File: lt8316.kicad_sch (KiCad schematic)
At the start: 37 parts

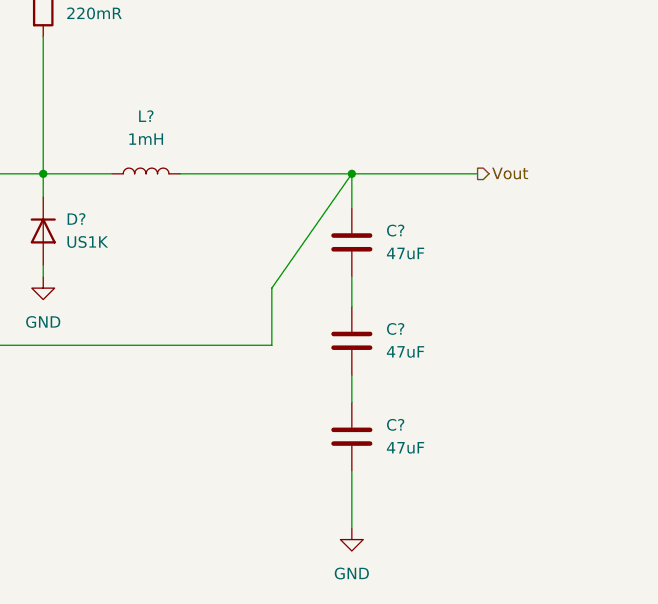
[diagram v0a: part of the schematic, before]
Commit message: gitignore change + capacitors improve
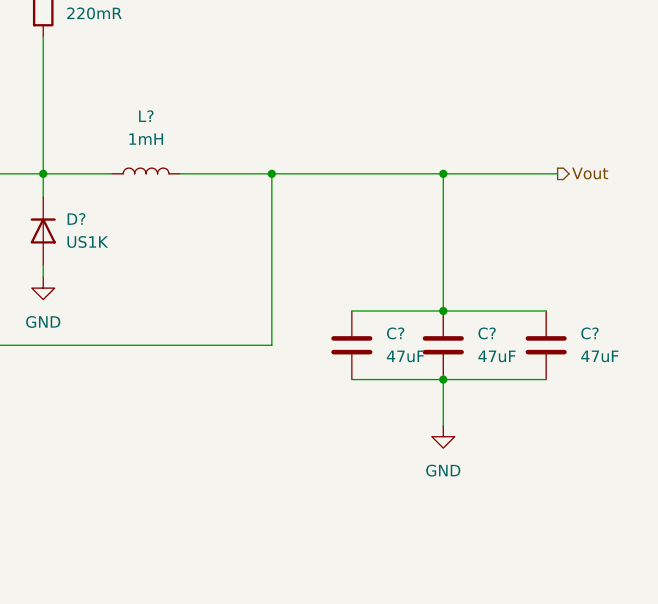
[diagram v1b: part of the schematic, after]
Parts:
- removed C?: 47uF, symbol Device:C
- added C?: 47uF, symbol Device:C
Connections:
- net GND: now also C?.2, C?.2
- net Vout: now also C?.1, C?.1
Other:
- moved on the sheet: C?

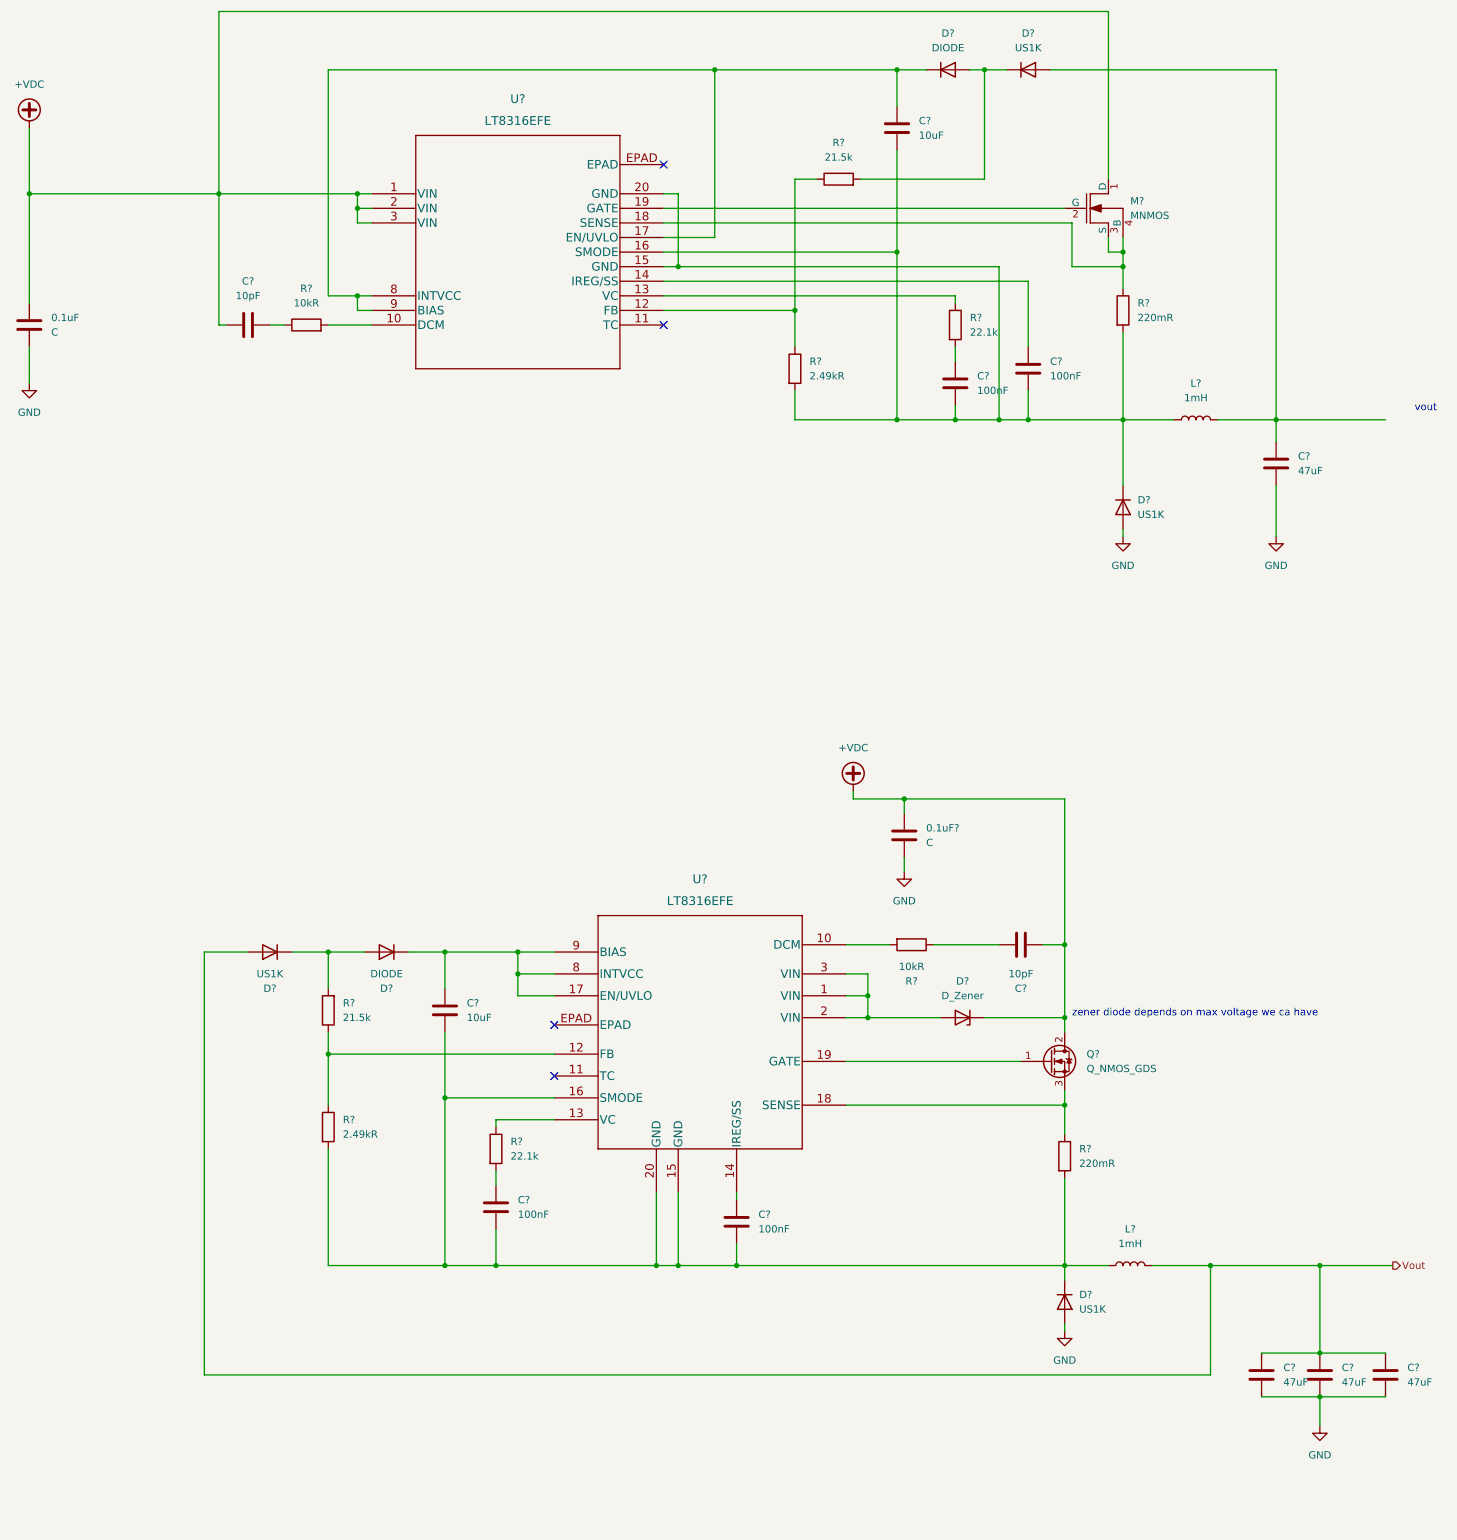
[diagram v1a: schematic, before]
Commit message: dodaję fus, wybieram led, zmieniam komparator, dodaję datasheety
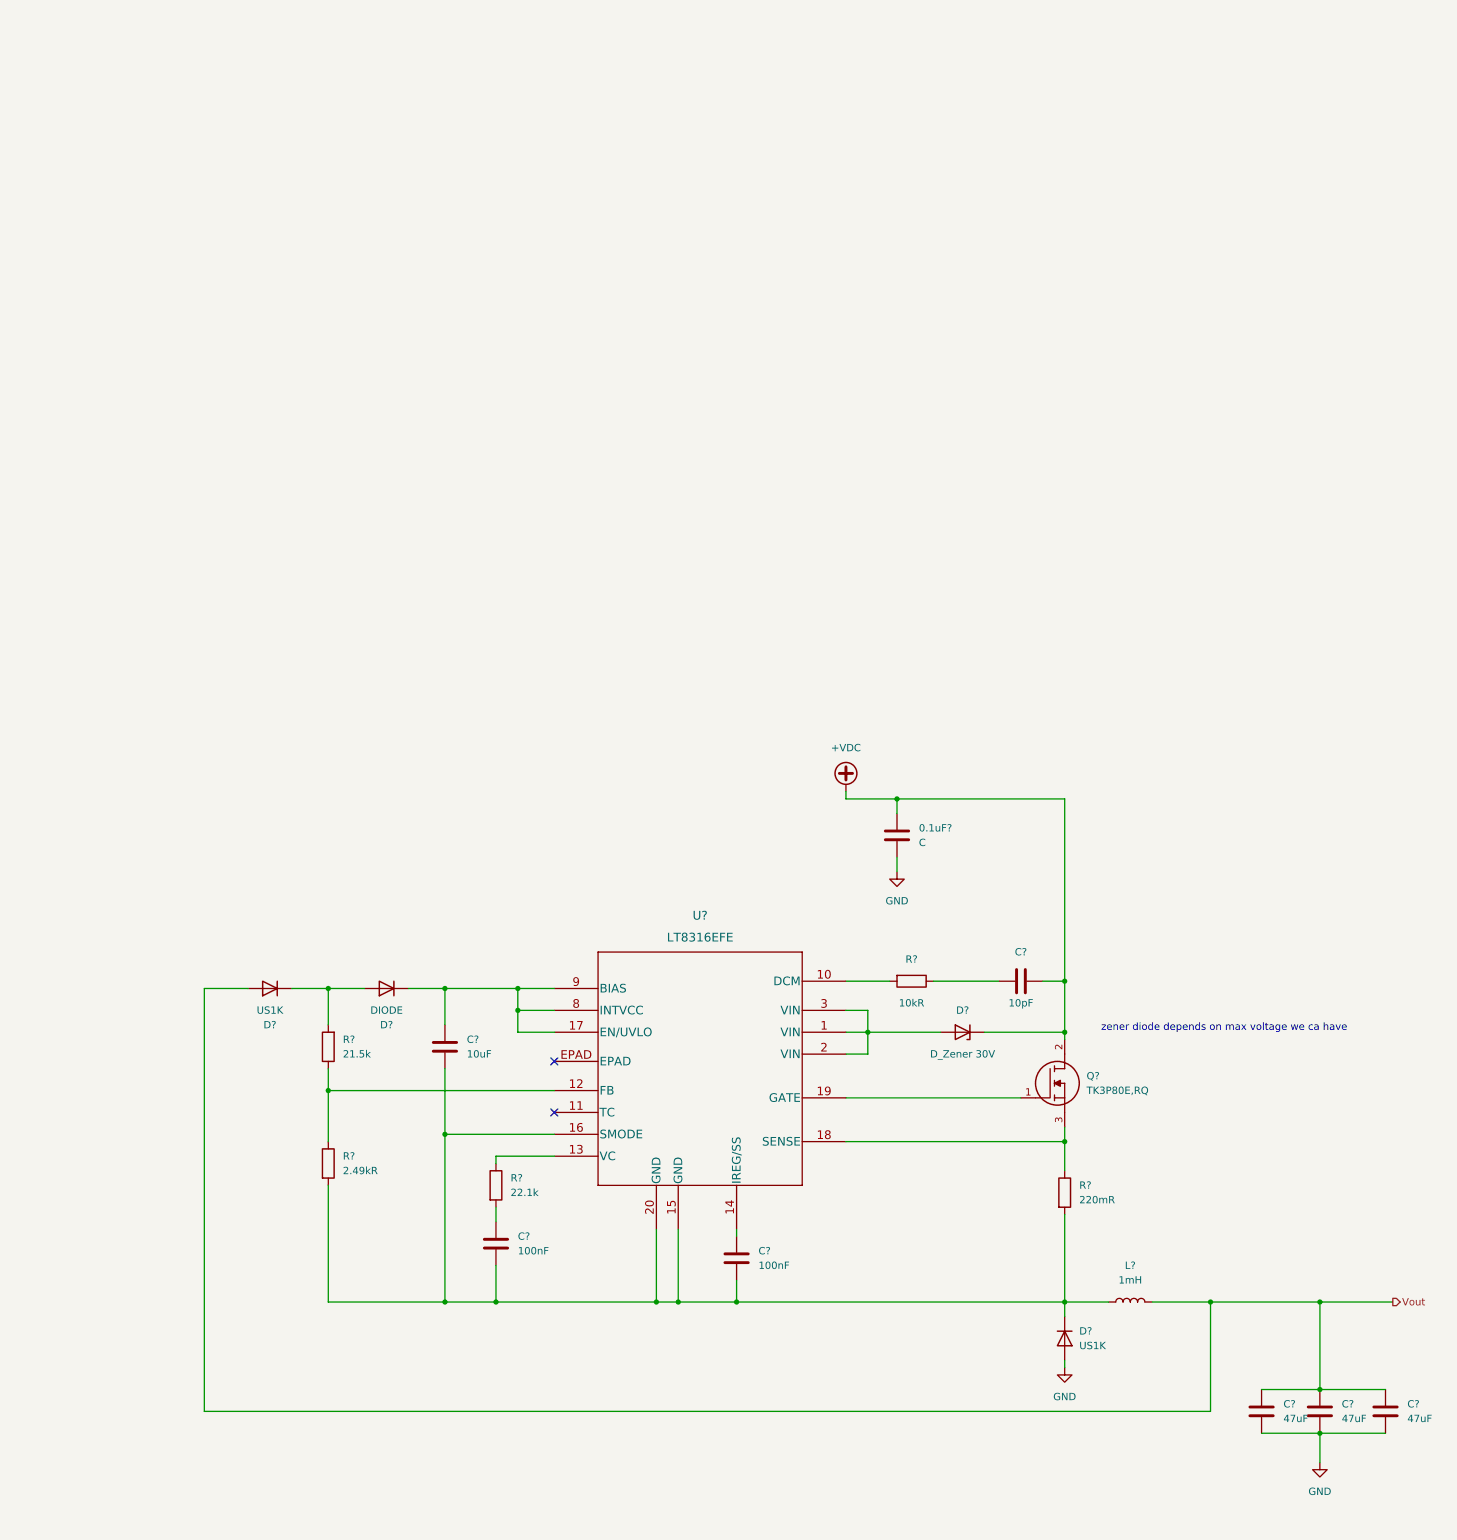
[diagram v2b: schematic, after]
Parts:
- removed 0.1uF: C, symbol Device:C
- removed C?: 47uF, symbol Device:C
- removed C? (x2): 100nF, symbol Device:C
- removed C?: 10pF, symbol Device:C
- removed C?: 10uF, symbol Device:C
- removed D? (x2): US1K, Diode_SMD:D_SMA, symbol Diode:US1K
- removed D?: DIODE, symbol Simulation_SPICE:DIODE
- removed L?: 1mH, symbol Device:L
- removed M?: MNMOS, symbol pspice:MNMOS
- removed Q?: Q_NMOS_GDS, symbol Device:Q_NMOS_GDS
- removed R?: 2.49kR, symbol Device:R
- removed R?: 22.1k, symbol Device:R
- removed R?: 10kR, symbol Device:R
- removed R?: 220mR, symbol Device:R
- removed R?: 21.5k, symbol Device:R
- removed U?: LT8316EFE, TSSOP20_FE_BB_16_, symbol Library_indicator:LT8316EFE
- added Q?: TK3P80E,RQ, TK3P80ERQ, symbol Voltage_indicator:TK3P80E,RQ
- D?: value D_Zener -> D_Zener 30V; footprint (none) -> Diode_SMD:D_SOD-123
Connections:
- net +VDC: now also Q?.2
- net at R?.1, U?.18 (SENSE): now also Q?.3
- net at U?.19 (GATE): now also Q?.1
- no-connect marks 4 -> 2
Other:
- note removed: "vout"
- moved on the sheet: 0.1uF?, C?, D?, L?, R?, U?

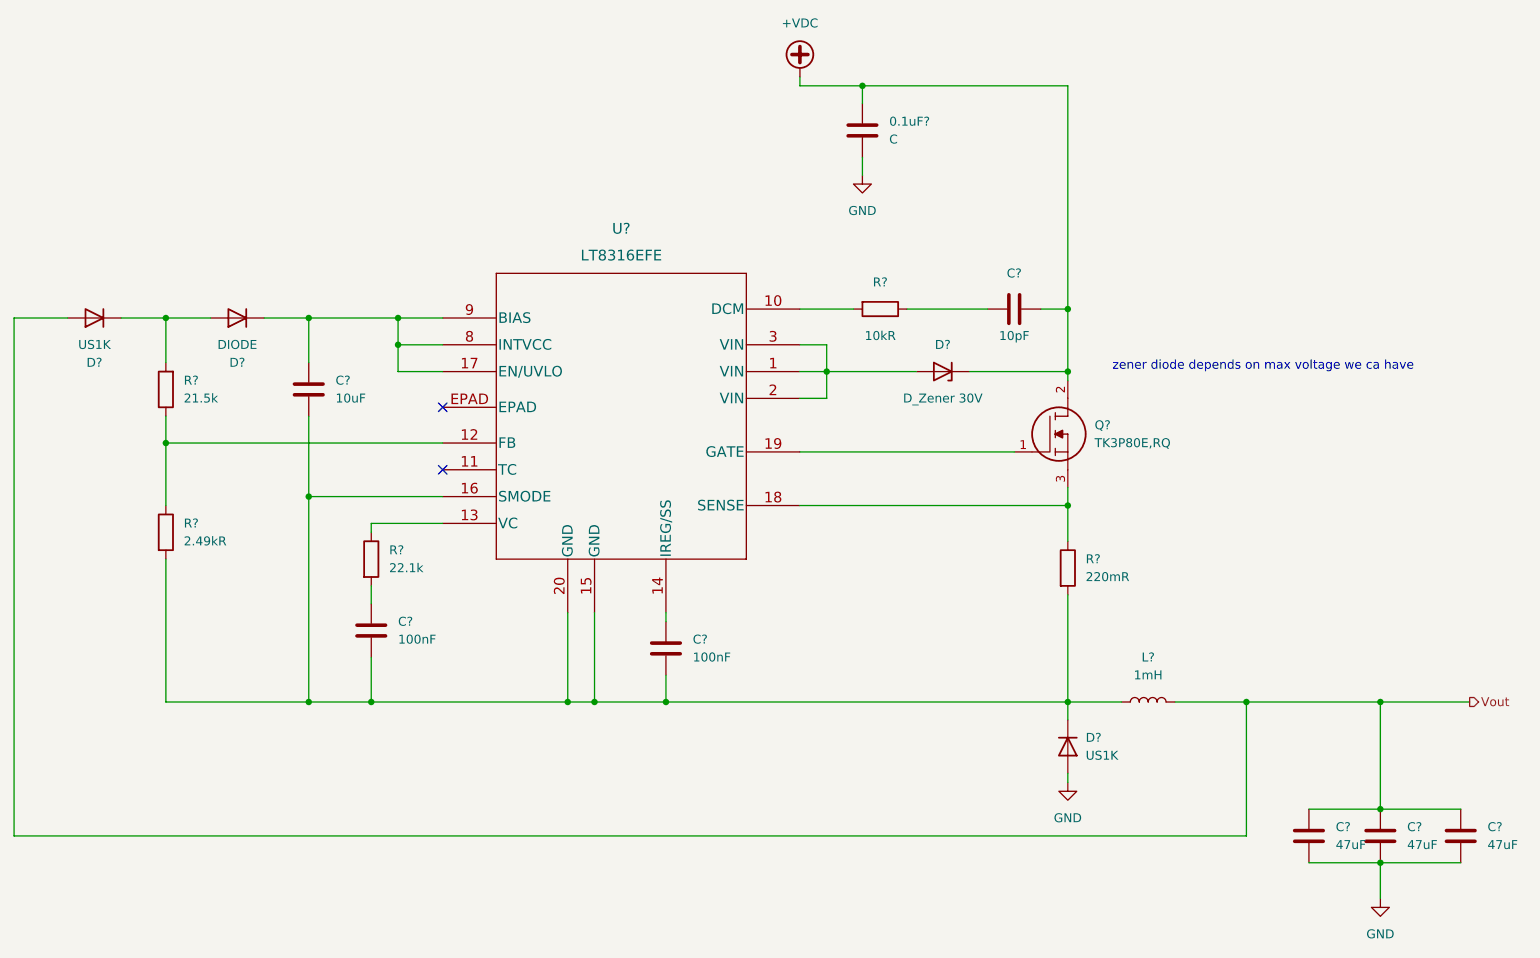
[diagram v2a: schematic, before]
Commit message: add resistors / add footprints and datasheets/ change symbols
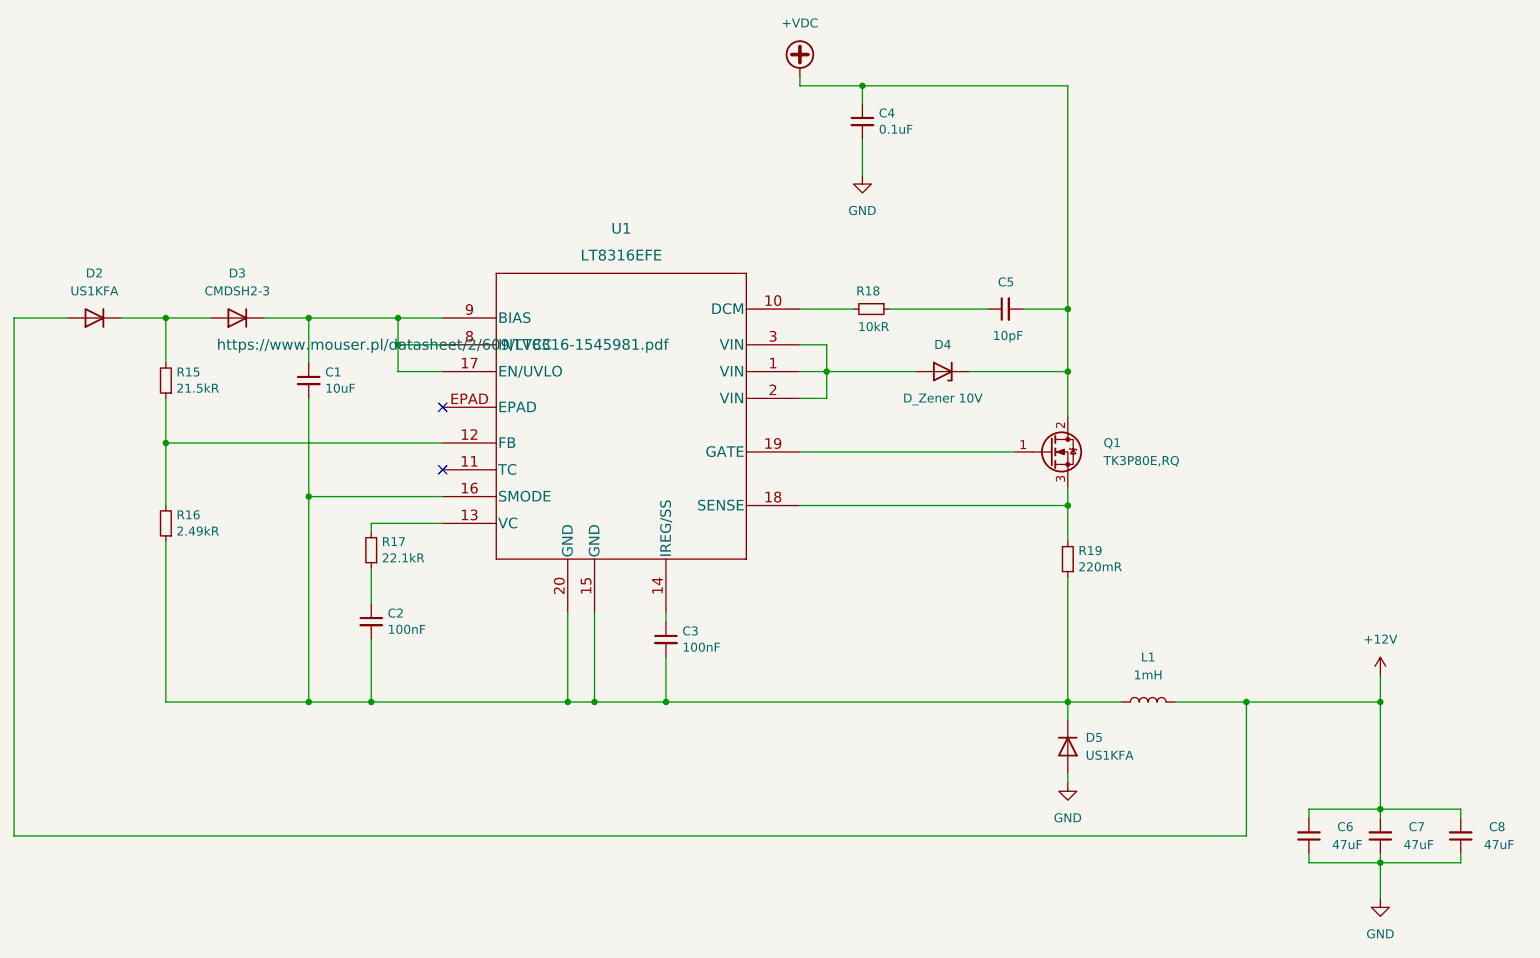
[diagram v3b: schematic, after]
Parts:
- removed 0.1uF?: C, symbol Device:C
- removed C?: 10pF, symbol Device:C
- removed C?: 10uF, symbol Device:C
- removed C? (x3): 47uF, symbol Device:C
- removed C? (x2): 100nF, symbol Device:C
- removed D?: US1K, Diode_SMD:D_SMA, symbol Diode:US1K
- removed R?: 21.5k, symbol Device:R
- removed R?: 220mR, symbol Device:R
- removed R?: 2.49kR, symbol Device:R
- removed R?: 10kR, symbol Device:R
- removed R?: 22.1k, symbol Device:R
- added C1: 10uF, Capacitor_SMD:C_1206_3216Metric, symbol Device:C_Small
- added C2, C3: 100nF, Capacitor_SMD:C_1206_3216Metric, symbol Device:C_Small
- added C4: 0.1uF, Capacitor_SMD:C_1206_3216Metric, symbol Device:C_Small
- added C5: 10pF, Capacitor_SMD:C_1206_3216Metric, symbol Device:C_Small
- added C6, C7, C8: 47uF, Capacitor_SMD:C_1206_3216Metric, symbol Device:C_Small
- added D5: US1KFA, Diode_SMD:D_SOD-123F, symbol Diode:US1K
- added R15: 21.5kR, Resistor_SMD:R_1206_3216Metric, symbol Device:R_Small
- added R16: 2.49kR, Resistor_SMD:R_1206_3216Metric, symbol Device:R_Small
- added R17: 22.1kR, Resistor_SMD:R_1206_3216Metric, symbol Device:R_Small
- added R18: 10kR, Resistor_SMD:R_1206_3216Metric, symbol Device:R_Small
- added R19: 220mR, Resistor_SMD:R_1206_3216Metric, symbol Device:R_Small
- D2: renamed from D?; value US1K -> US1KFA; footprint Diode_SMD:D_SMA -> Diode_SMD:D_SOD-123F
- D3: renamed from D?; value DIODE -> CMDSH2-3; footprint (none) -> Diode_SMD:D_SOD-323
- D4: renamed from D?; value D_Zener 30V -> D_Zener 10V; footprint Diode_SMD:D_SOD-123 -> Diode_SMD:D_SOD-523
- L1: renamed from L?; footprint (none) -> Inductor_SMD:L_Wuerth_WE-PD2-Typ-MS
- Q1: renamed from Q?; footprint TK3P80ERQ -> Package_TO_SOT_SMD:TO-252-2; symbol Voltage_indicator:TK3P80E,RQ -> Device:Q_NMOS_GDS
- U1: renamed from U?; footprint TSSOP20_FE_BB_16_ -> Package_SO:TSSOP-20_4.4x6.5mm_P0.65mm
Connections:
- net +VDC: now also C4.1, C5.2
- net GND: now also C4.2, C6.1, C7.1, C8.1, D5.2 (A)
- net at U1.12 (FB): now also R15.1, R16.2
- net at D2.1 (K), D3.1 (A): now also R15.2
- net at Q1.3 (S), U1.18 (SENSE): now also R19.2
- net at L1.1, U1.15 (GND), U1.16 (SMODE)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: now also C1.2, C2.2, C3.2, D5.1 (K), R16.1, R19.1
- net at U1.10 (DCM): now also R18.2
- net at U1.13 (VC): now also R17.2
- net at U1.14 (IREG/SS): now also C3.1
- net at D3.2 (K), U1.17 (EN/UVLO), U1.8 (INTVCC)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: now also C1.1
- net Vout renamed +12V
- net +12V: now also C6.2, C7.2, C8.2
- new net: C2.1, R17.1
- new net: C5.1, R18.1
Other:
- note removed: "zener diode depends on max voltage we ca have"

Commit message: add pcb
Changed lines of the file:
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@@
     )
     (property "Datasheet" "https://www.mouser.pl/datasheet/2/609/LT8316-1545981.pdf" (id 3) (at 116.84 66.04 0)
-      (effects (font (size 1.524 1.524)))
+      (effects (font (size 1.524 1.524)) hide)
     )
     (pin "1")
